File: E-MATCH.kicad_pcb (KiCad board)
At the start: 2 copper layers, 7 parts, among them IC1 NCV81071BZR2G, J2 691137710002, Q2 AOSP36326C, U1 TMCS1108A2UQDR

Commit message: More 3-d models
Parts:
- moved CR1 9.55 mm to (174.5, 100.5)
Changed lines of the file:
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@@
 		)
 		(embedded_fonts no)
+		(model "${KIPRJMOD}/Custom E-CAD Models/Mosfet/AOSP36326C.step"
+			(offset
+				(xyz 0 0 0)
+			)
+			(scale
+				(xyz 1 1 1)
+			)
+			(rotate
+				(xyz -90 -0 -0)
+			)
+		)
 	)
 	(footprint "Gate Driver:SOP65P490X110-9N"
@@
 		)
 		(embedded_fonts no)
-		(model "NCV81071BZR2G.stp"
+		(model "${KIPRJMOD}/Custom E-CAD Models/Hall Effect Current Sensor/TMCS1108A2UQDR.step"
 			(offset
 				(xyz 0 0 0)
 			)
 			(scale
-				(xyz 1 1 1)
+				(xyz 0.9 0.8 0.5)
 			)
 			(rotate
-				(xyz 0 0 0)
+				(xyz -90 -0 -0)
 			)
 		)
@@
 		)
 		(embedded_fonts no)
+		(model "${KIPRJMOD}/Custom E-CAD Models/Gate_Resistor/RC1206FR-1310RL.step"
+			(offset
+				(xyz 0 0 0)
+			)
+			(scale
+				(xyz 1 1 1)
+			)
+			(rotate
+				(xyz 90 -180 -0)
+			)
+		)
 	)
 	(footprint "Module:Arduino_Nano"
@@
 	(footprint "Schottcky Diode:DIODE_MSP3V3"
 		(layer "F.Cu")
-		(at 164.9598 99.5)
+		(at 174.4598 100.5)
 		(tags "MSS1P5-M3/89A ")
 		(property "Reference" "CR1"
@@
 			(polygon
 				(pts
-					(xy 164.9598 98.8523) (xy 165.4932 98.8523) (xy 165.4932 100.1477) (xy 164.9598 100.1477)
+					(xy 174.4598 99.8523) (xy 174.9932 99.8523) (xy 174.9932 101.1477) (xy 174.4598 101.1477)
 				)
 			)
 		)
 		(embedded_fonts no)
+		(model "${KIPRJMOD}/Custom E-CAD Models/Schottky Diode/MSS1P5-M3:89A/MSMP package.step"
+			(offset
+				(xyz 0.5 0.25 0)
+			)
+			(scale
+				(xyz 1 1 1)
+			)
+			(rotate
+				(xyz -90 -0 -0)
+			)
+		)
 	)
 	(embedded_fonts no)

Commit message: linked 3-d models
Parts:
- removed J2: 691137710002, Screw_Terminal_0102:691137710002
- added J1: 691210910002, Screw_Terminal:691210910002, F.Cu at (146.7, 114.5)
- moved IC1 39.1 mm to (145.4, 87.9)
- moved CR1 29.2 mm to (146.0, 107.0), turned to 180 degrees
- moved A1 24.3 mm to (164.5, 76.9)
- moved U1 22.8 mm to (145.3, 79.5)
- moved Q2 18.3 mm to (146.6, 100.2), turned to -90 degrees
- moved R1 15.0 mm to (146.1, 94.5)
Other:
- board outline added: 50 x 50 mm

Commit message: A lot of changes :)
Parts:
- added CR2: MSS1P5-M3/89A, Schottcky Diode:DIODE_MSP3V3, F.Cu at (188.0, 84.3)
- added CR3: MSS1P5-M3/89A, Schottcky Diode:DIODE_MSP3V3, F.Cu at (188.0, 87.1)
- added CR4: MSS1P5-M3/89A, Schottcky Diode:DIODE_MSP3V3, F.Cu at (188.0, 89.9)
- added IC2: NCV81071BZR2G, Gate Driver:SOP65P490X110-9N, F.Cu at (193.8, 87.0)
- added J2: 691210910002, Screw_Terminal:691210910002, F.Cu at (182.7, 76.0)
- added J3: 691210910002, Screw_Terminal:691210910002, F.Cu at (189.9, 76.0)
- added J4: 691210910002, Screw_Terminal:691210910002, F.Cu at (197.1, 76.0)
- added Q1: AOSP36326C, N-Ch Mosfet:SO8SOP-8L_AOS, F.Cu at (176.3, 83.4)
- added Q3: AOSP36326C, N-Ch Mosfet:SO8SOP-8L_AOS, F.Cu at (176.3, 96.7)
- added Q4: AOSP36326C, N-Ch Mosfet:SO8SOP-8L_AOS, F.Cu at (176.3, 103.4)
- added R2: 10R, Gate Resistor:RES_RC1206_YAG, F.Cu at (183.2, 85.1)
- added R3: 10R, Gate Resistor:RES_RC1206_YAG, F.Cu at (183.2, 88.5)
- added R4: 10R, Gate Resistor:RES_RC1206_YAG, F.Cu at (183.2, 91.8)
- IC1: footprint Current Sensor:D0008A-IPC_A -> Gate Driver:SOP65P490X110-9N
- R1: value R -> 10R
- U1: footprint Gate Driver:SOP65P490X110-9N -> Current Sensor:D0008A-MFG
- moved CR1 49.2 mm to (188.0, 81.5), turned to 0 degrees
- moved IC1 48.7 mm to (193.8, 82.4)
- moved J1 48.1 mm to (175.6, 76.0)
- moved U1 43.5 mm to (185.3, 96.6)
- moved R1 39.2 mm to (183.2, 81.7)
- moved Q2 31.4 mm to (176.3, 90.0), turned to 0 degrees
- moved A1 9.81 mm to (154.7, 76.4)
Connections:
- IC1 pad 6: unconnected-(IC1-OUTB-Pad6) -> Gate_Drive2
- IC1 pad 7: Net-(IC1-OUTA) -> Gate_Drive1
- Q2 pad 5: Net-(CR1-Pad2) -> Net-(CR2-Pad2)
- Q2 pad 6: Net-(CR1-Pad2) -> Net-(CR2-Pad2)
- Q2 pad 7: Net-(CR1-Pad2) -> Net-(CR2-Pad2)
- Q2 pad 8: Net-(CR1-Pad2) -> Net-(CR2-Pad2)
- R1 pad 1: Net-(Q2-Pad4) -> Net-(Q1-Pad4)
- R1 pad 2: Net-(IC1-OUTA) -> unconnected-(R1-Pad2)
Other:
- board outline removed

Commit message: routing
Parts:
- added J5: DC Jack, DC-Jack:TENSILITY_54-00130, F.Cu at (184.3, 71.0)
- moved Q3 47.2 mm to (192.0, 52.3)
- moved Q4 47.2 mm to (192.0, 58.9)
- moved Q2 47.2 mm to (192.0, 45.6)
- moved Q1 47.2 mm to (192.0, 38.9)
- moved J1 46.5 mm to (202.8, 38.3), turned to -90 degrees
- moved CR1 44.3 mm to (197.8, 38.2), turned to 90 degrees
- moved R1 40.7 mm to (184.9, 41.0), turned to 180 degrees
- moved IC1 40.4 mm to (180.5, 44.2)
- moved CR2 40.0 mm to (197.8, 45.5), turned to 90 degrees
- moved R2 37.6 mm to (184.9, 47.5), turned to 180 degrees
- moved J2 36.5 mm to (202.8, 45.4), turned to -90 degrees
- moved CR3 35.7 mm to (197.9, 52.7), turned to 90 degrees
- moved R3 34.0 mm to (184.9, 54.5), turned to 180 degrees
- moved IC2 32.2 mm to (180.6, 57.7)
- moved U1 31.6 mm to (195.0, 66.4), turned to 180 degrees
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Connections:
- A1 pad 10: Enable_Signal -> unconnected-(A1-D7-Pad10)
- A1 pad 11: unconnected-(A1-D8-Pad11) -> Enable_Signal4
- A1 pad 12: unconnected-(A1-D9-Pad12) -> Enable_Signal3
- A1 pad 13: unconnected-(A1-D10-Pad13) -> Enable_Signal2
- A1 pad 14: unconnected-(A1-D11-Pad14) -> Enable_Signal1
- A1 pad 5: unconnected-(A1-D2-Pad5) -> Trigger_Signal4
- A1 pad 6: unconnected-(A1-D3-Pad6) -> Trigger_Signal3
- A1 pad 7: unconnected-(A1-D4-Pad7) -> Trigger_Signal2
- A1 pad 8: Trigger_Signal -> Trigger_Signal1
- IC1 pad 1: Enable_Signal -> Enable_Signal1
- IC1 pad 2: Trigger_Signal -> Trigger_Signal1
- IC1 pad 3: GND -> Enable_Signal2
- IC1 pad 4: GND -> Trigger_Signal2
- IC2 pad 1: Enable_Signal -> Enable_Signal3
- IC2 pad 2: Trigger_Signal -> Trigger_Signal3
- IC2 pad 3: GND -> Enable_Signal4
- IC2 pad 4: GND -> Trigger_Signal4
- R1 pad 2: unconnected-(R1-Pad2) -> Gate_Drive1
- R2 pad 2: unconnected-(R2-Pad2) -> Gate_Drive2
- R3 pad 2: unconnected-(R3-Pad2) -> Gate_Drive3
- R4 pad 2: unconnected-(R4-Pad2) -> Gate_Drive4
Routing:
- net Net-(CR1-Pad1): track 0.00 -> 64.5 mm
- net Sensor_Output: track 0.00 -> 43.9 mm
- net 5V: track 0.00 -> 34.6 mm
- net GND: track 0.00 -> 26.7 mm, vias 0 -> 15
- net Trigger_Signal2: track 0.00 -> 17.6 mm, vias 0 -> 1
- net Trigger_Signal1: track 0.00 -> 15.8 mm, vias 0 -> 1
- net Net-(CR4-Pad2): track 0.00 -> 12.7 mm
- net Net-(CR2-Pad2): track 0.00 -> 12.1 mm
- net Net-(CR1-Pad2): track 0.00 -> 12.0 mm
- net Net-(CR3-Pad2): track 0.00 -> 12.0 mm
- net Enable_Signal3: track 0.00 -> 11.2 mm
- net Enable_Signal4: track 0.00 -> 10.7 mm
- net Trigger_Signal3: track 0.00 -> 9.71 mm, vias 0 -> 1
- net Trigger_Signal4: track 0.00 -> 7.79 mm
- net Enable_Signal1: track 0.00 -> 4.31 mm
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- added copper zone on B.Cu, net GND
- added copper zone on F.Cu, net Net-(CR1-Pad2)
- added copper zone on F.Cu, net VBAT
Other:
- board outline added: 50.8 x 45.5 mm

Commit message: Led-indicator file structure
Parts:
- moved IC1 0.50 mm to (181.0, 44.2)

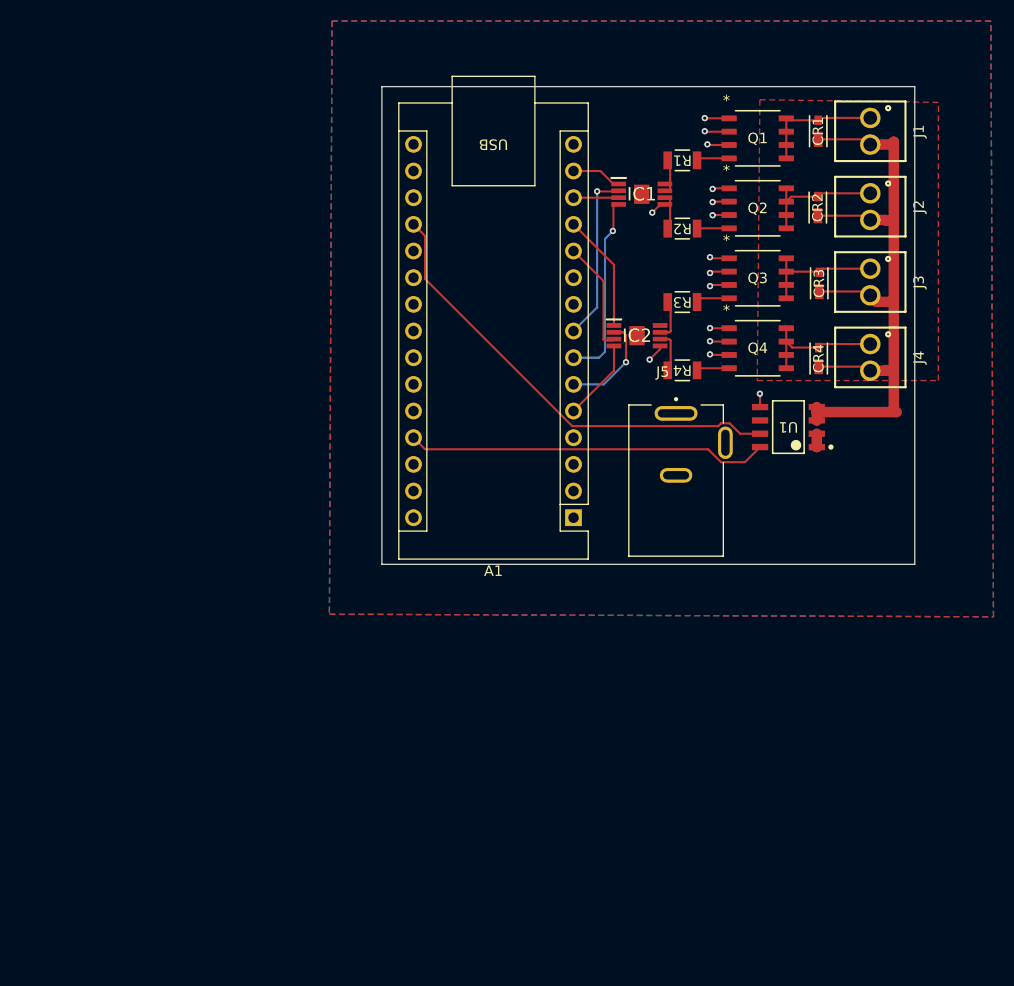
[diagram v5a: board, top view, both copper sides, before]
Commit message: 2 layers to 4 layers
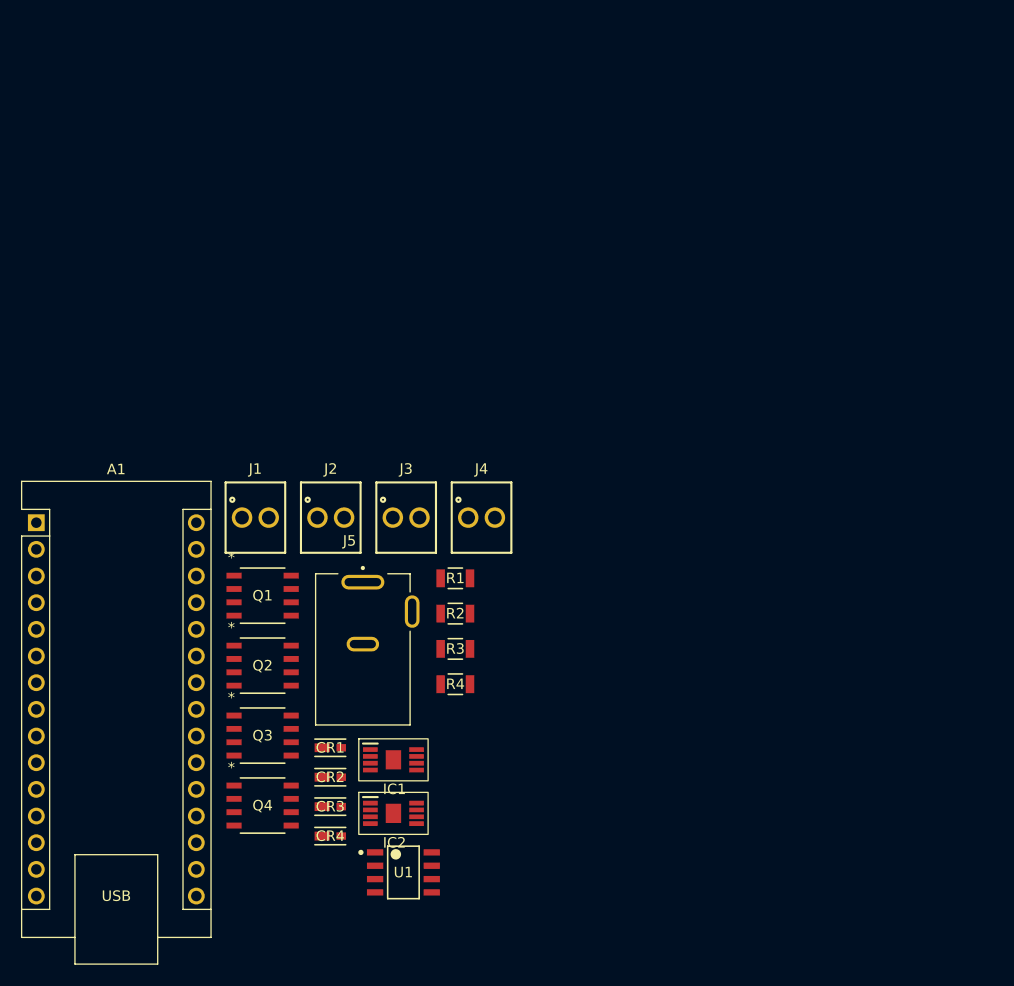
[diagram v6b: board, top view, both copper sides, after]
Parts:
- moved CR1 74.9 mm to (151.3, 97.0), turned to 0 degrees
- moved CR2 71.4 mm to (151.3, 99.8), turned to 0 degrees
- moved J1 69.2 mm to (144.2, 75.0), turned to 0 degrees
- moved CR3 68.2 mm to (151.3, 102.6), turned to 0 degrees
- moved CR4 65.1 mm to (151.3, 105.4), turned to 0 degrees
- moved Q3 64.2 mm to (144.9, 95.8)
- moved Q2 64.2 mm to (144.9, 89.1)
- moved Q4 64.2 mm to (144.9, 102.5)
- moved Q1 64.2 mm to (144.9, 82.5)
- moved J2 59.3 mm to (151.4, 75.0), turned to 0 degrees
- moved IC1 58.8 mm to (157.3, 98.1)
- moved U1 56.1 mm to (158.3, 108.8), turned to 0 degrees
- moved A1 51.2 mm to (123.3, 75.5), turned to 0 degrees
- moved IC2 51.1 mm to (157.3, 103.2)
- moved J3 49.6 mm to (158.6, 75.0), turned to 0 degrees
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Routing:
- net Net-(CR1-Pad1): track 64.5 -> 0.00 mm
- net Sensor_Output: track 43.9 -> 0.00 mm
- net 5V: track 34.6 -> 0.00 mm
- net GND: track 26.7 -> 0.00 mm, vias 15 -> 0
- net Trigger_Signal2: track 17.6 -> 0.00 mm, vias 1 -> 0
- net Trigger_Signal1: track 15.8 -> 0.00 mm, vias 1 -> 0
- net Net-(CR4-Pad2): track 12.7 -> 0.00 mm
- net Net-(CR2-Pad2): track 12.1 -> 0.00 mm
- net Net-(CR1-Pad2): track 12.0 -> 0.00 mm
- net Net-(CR3-Pad2): track 12.0 -> 0.00 mm
- net Enable_Signal3: track 11.2 -> 0.00 mm
- net Enable_Signal4: track 10.7 -> 0.00 mm
- net Trigger_Signal3: track 9.71 -> 0.00 mm, vias 1 -> 0
- net Trigger_Signal4: track 7.79 -> 0.00 mm
- net Enable_Signal1: track 4.31 -> 0.00 mm
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- removed copper zone on B.Cu, net GND
- removed copper zone on F.Cu, net Net-(CR1-Pad2)
- removed copper zone on F.Cu, net VBAT
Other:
- board outline removed
- copper layers 2 -> 4

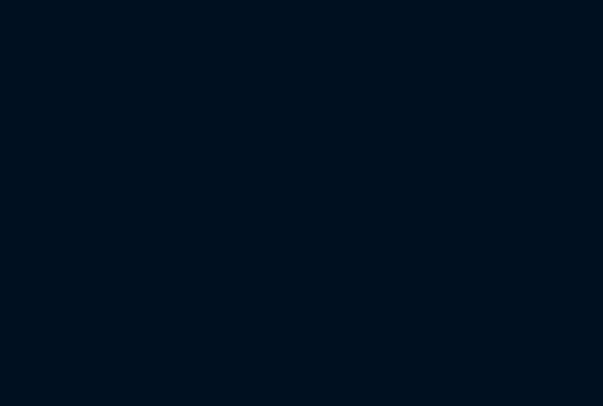
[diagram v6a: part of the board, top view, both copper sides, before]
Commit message: Added SMD-LED footprint
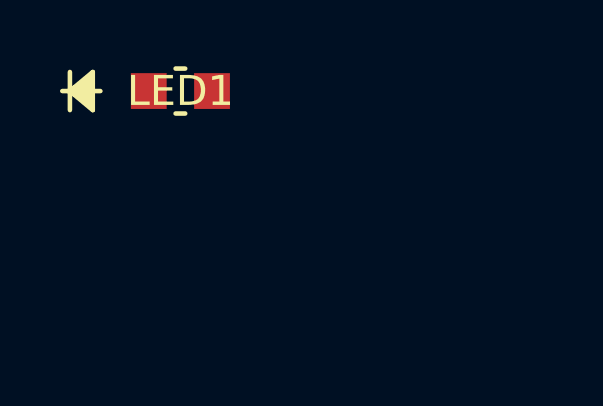
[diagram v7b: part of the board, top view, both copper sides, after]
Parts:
- added LED1: LTST-C170GKT, Smd_Led:LED_LTST-C170GKT_LTO, F.Cu at (4.01, 0.95)

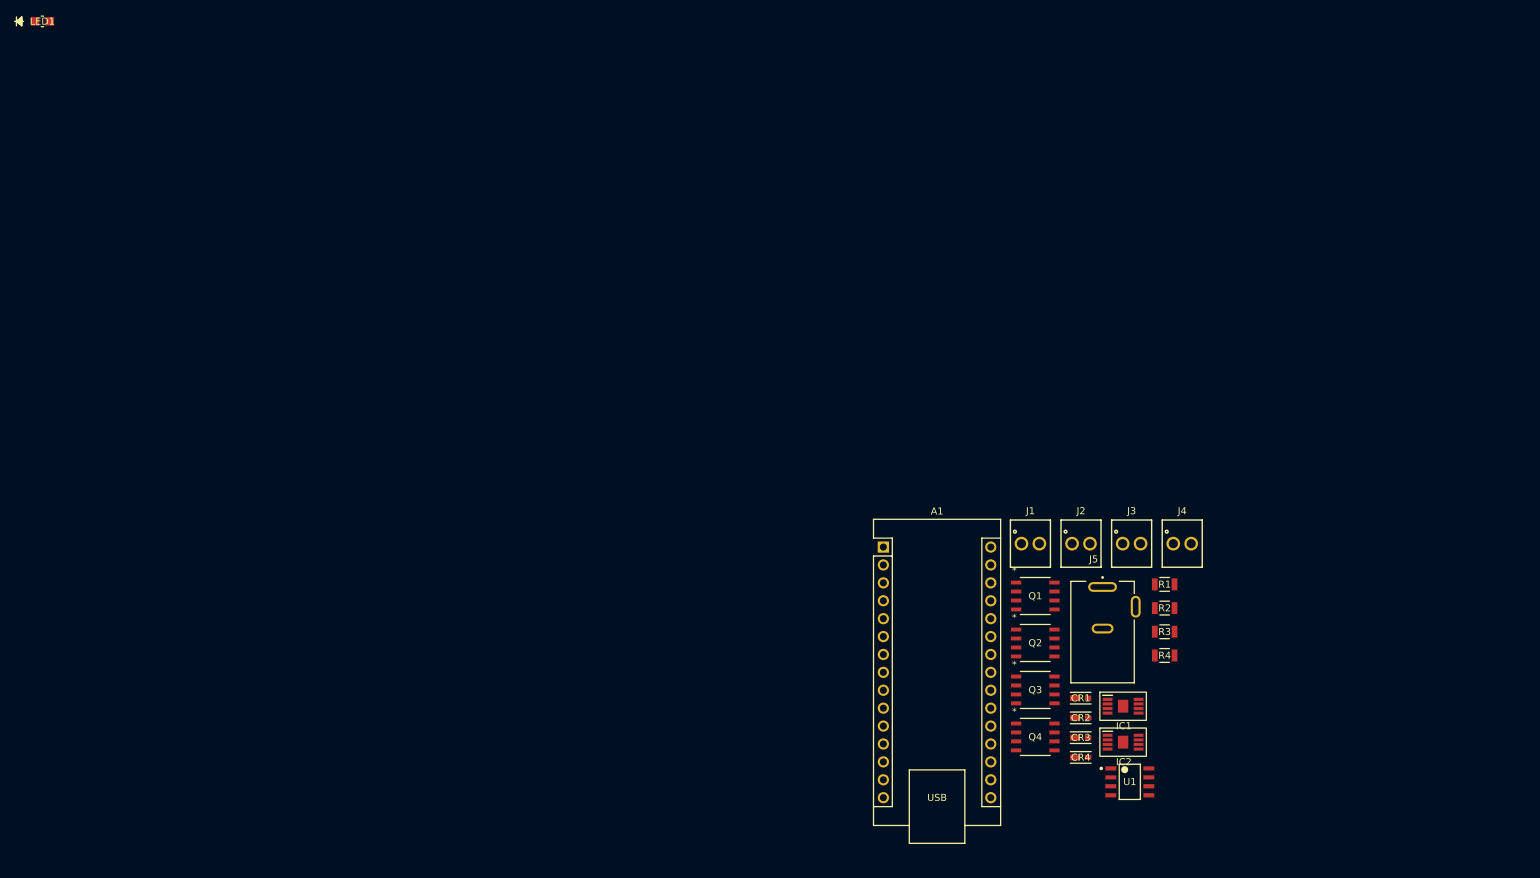
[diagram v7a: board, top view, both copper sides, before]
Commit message: edited current sensor symbol
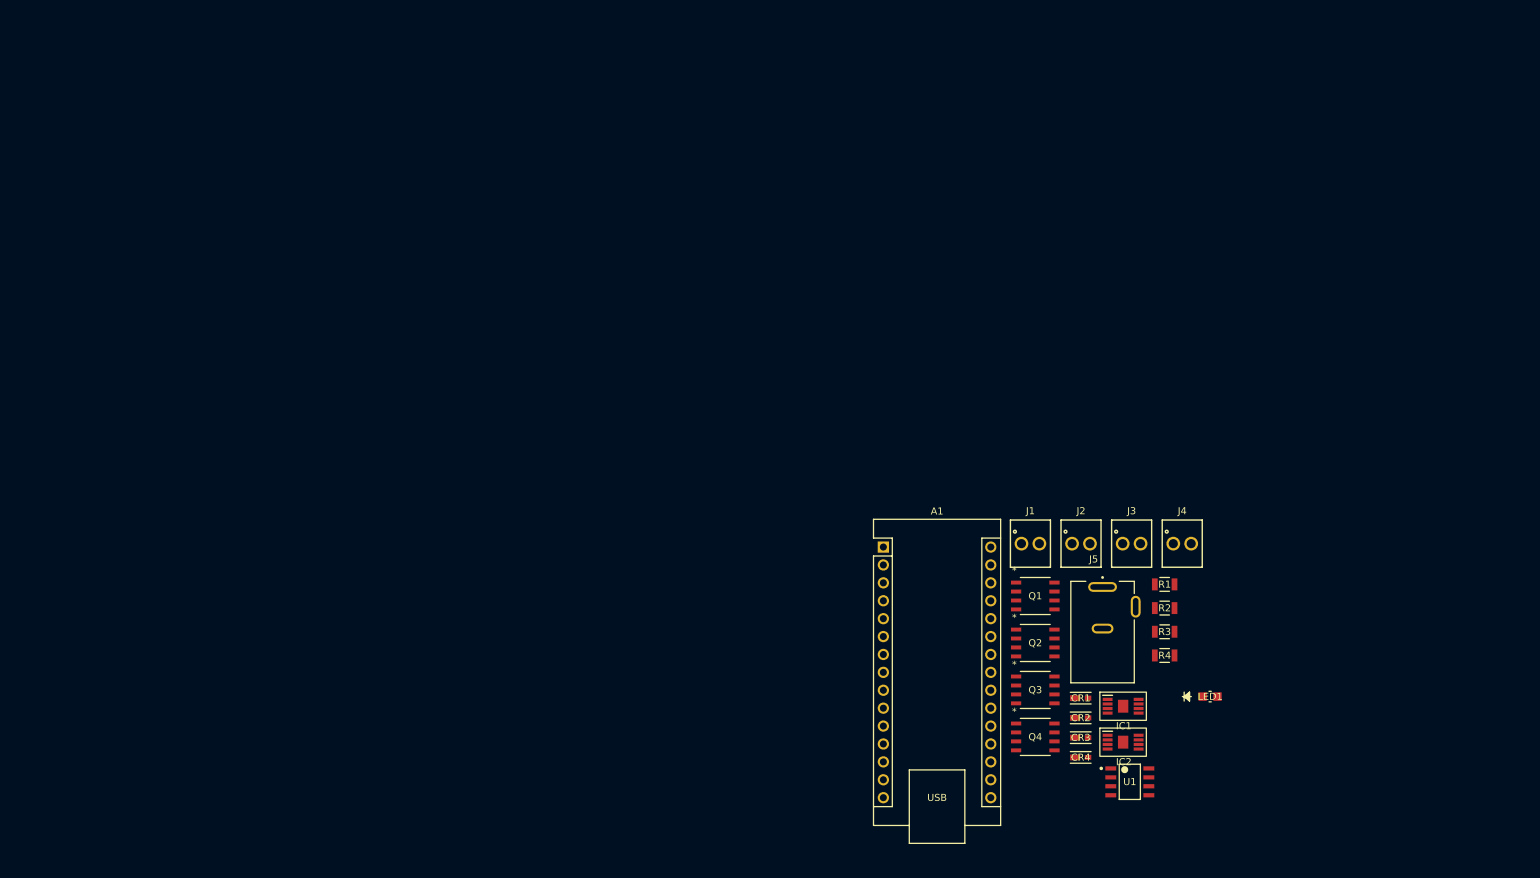
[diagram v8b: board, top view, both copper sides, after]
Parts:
- moved LED1 191.4 mm to (169.7, 96.8)
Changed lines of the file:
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@@
 	(footprint "Smd_Led:LED_LTST-C170GKT_LTO"
 		(layer "F.Cu")
-		(at 4.0132 0.9525)
+		(at 169.6959 96.75)
 		(tags "LTST-C170GKT ")
 		(property "Reference" "LED1"
@@
 			(polygon
 				(pts
-					(xy 3.6068 0.381) (xy 4.4196 0.381) (xy 4.4196 1.524) (xy 3.6068 1.524)
+					(xy 169.2895 96.1785) (xy 170.1023 96.1785) (xy 170.1023 97.3215) (xy 169.2895 97.3215)
 				)
 			)
 		)
 		(embedded_fonts no)
+		(model "${KIPRJMOD}/Custom E-CAD Models/3D Models/SMD-Led/LED_LTST-C170GKT_LTO.step"
+			(offset
+				(xyz 0 0 0)
+			)
+			(scale
+				(xyz 1 1 1)
+			)
+			(rotate
+				(xyz 0 0 0)
+			)
+		)
 	)
 	(embedded_fonts no)
